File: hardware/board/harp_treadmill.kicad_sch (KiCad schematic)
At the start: 1 part

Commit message: update schematic; continue pcb draft
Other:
- note removed: "TODO: consider 6V and 12V setting via resistors? We could buffer the feedback resistor value into the PICO's built-in ADC."
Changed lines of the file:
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@@
     (stroke (width 0) (type default))
-  )
-  (text "TODO: consider 6V and 12V setting via resistors?\n    We could buffer the feedback resistor value into the\n    PICO's built-in ADC."
-    (at 118.11 130.81 0)
-    (effects (font (size 1.27 1.27)) (justify left bottom))
   )
   (text "Ground Lug" (at 222.25 125.984 0)
@@
   )
   (symbol (lib_id "power:GND") (at 226.822 134.62 0) (unit 1)
-    (in_bom yes) (on_board yes) (dnp no) (fields_autoplaced)
+    (in_bom yes) (on_board yes) (dnp no)
     (property "Reference" "#PWR0127" (at 226.822 140.97 0)
       (effects (font (size 1.27 1.27)) hide)
     )
-    (property "Value" "GND" (at 226.822 139.7 0)
+    (property "Value" "GND" (at 226.822 138.43 0)
       (effects (font (size 1.27 1.27)))
     )

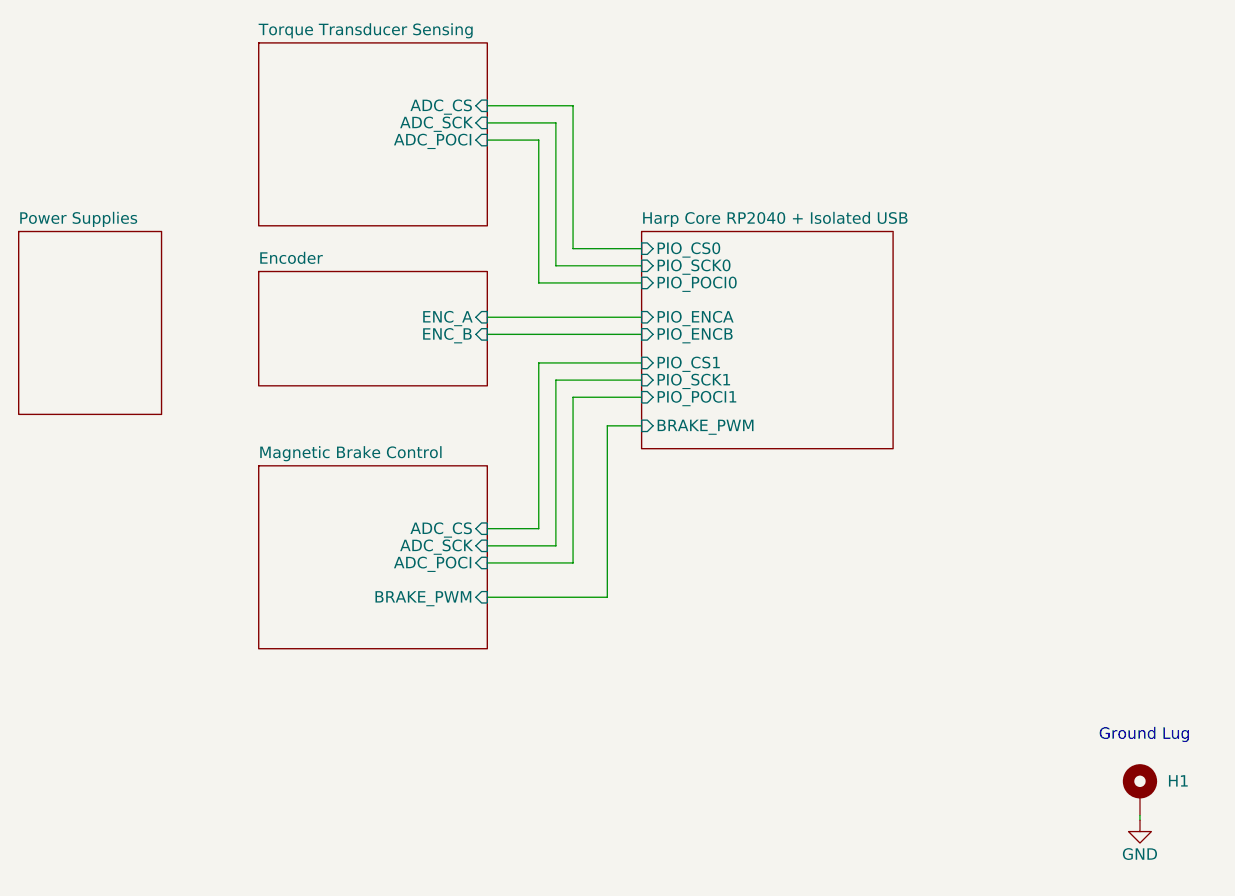
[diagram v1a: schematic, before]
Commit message: draft layout with analog brake driver circuit
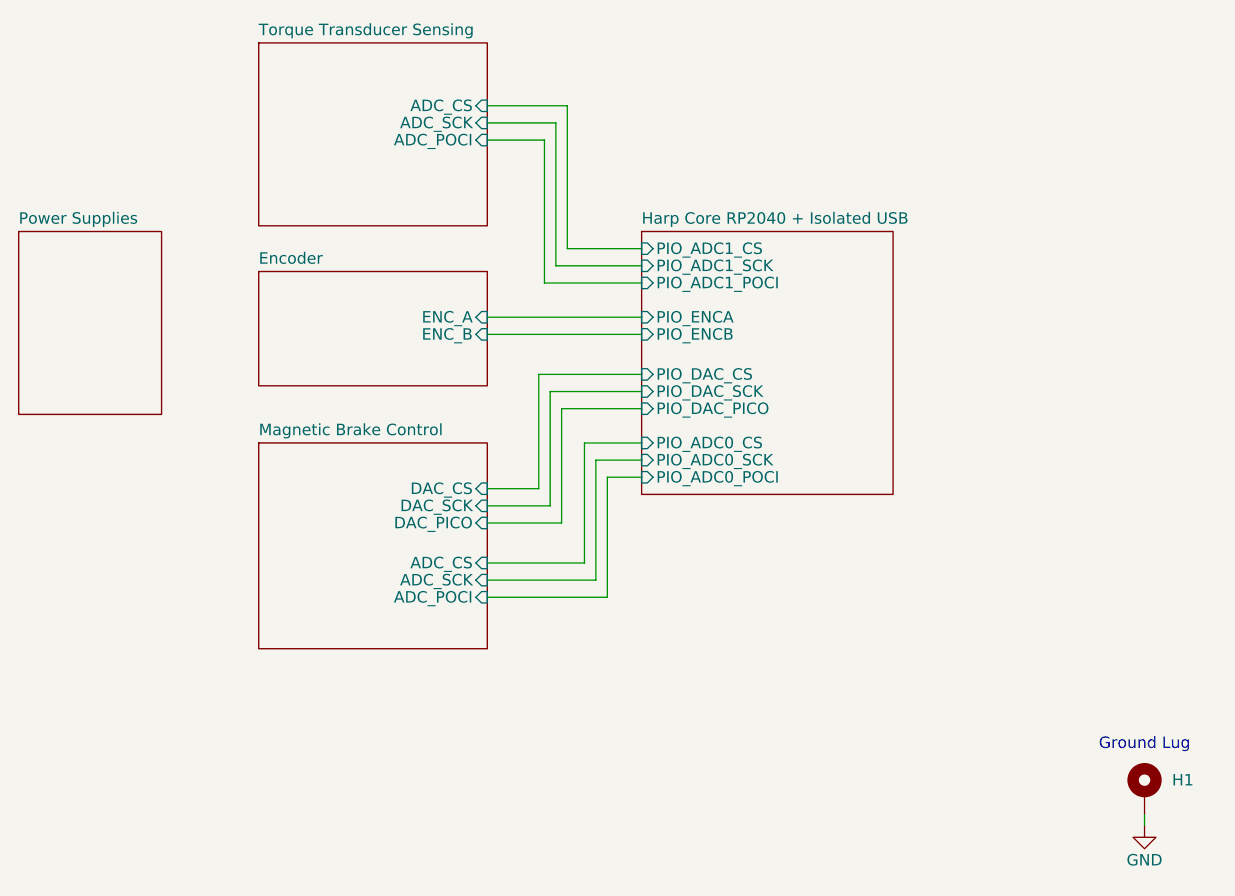
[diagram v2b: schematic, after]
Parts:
- H1: Link (none) -> n/a; Manufacturer (none) -> n/a; Manufacturer Number (none) -> n/a
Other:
- sheet Harp Core RP2040 + Isolated USB ports: added PIO_ADC0_CS, PIO_ADC0_POCI, PIO_ADC0_SCK, PIO_ADC1_CS, PIO_ADC1_POCI, PIO_ADC1_SCK, PIO_DAC_CS, PIO_DAC_PICO, PIO_DAC_SCK; removed BRAKE_PWM, PIO_CS0, PIO_CS1, PIO_POCI0, PIO_POCI1, PIO_SCK0, PIO_SCK1
- sheet Magnetic Brake Control ports: added DAC_CS, DAC_PICO, DAC_SCK; removed BRAKE_PWM
- moved on the sheet: H1

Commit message: draft v0.1 pcb
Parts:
- H1: Link n/a -> https://www.digikey.com/en/products/detail/keystone-electro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; Manufacturer n/a -> Keystone Electronics; Manufacturer Number n/a -> 7794
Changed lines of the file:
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@@
       (effects (font (size 1.27 1.27)) hide)
     )
-    (property "Link" "n/a" (at 227.33 131.445 0)
+    (property "Link" "https://www.digikey.com/en/products/detail/keystone-electronics/7794/2171012" (at 227.33 131.445 0)
       (effects (font (size 1.27 1.27)) hide)
     )
-    (property "Manufacturer" "n/a" (at 227.33 131.445 0)
+    (property "Manufacturer" "Keystone Electronics" (at 227.33 131.445 0)
       (effects (font (size 1.27 1.27)) hide)
     )
-    (property "Manufacturer Number" "n/a" (at 227.33 131.445 0)
+    (property "Manufacturer Number" "7794" (at 227.33 131.445 0)
       (effects (font (size 1.27 1.27)) hide)
     )
